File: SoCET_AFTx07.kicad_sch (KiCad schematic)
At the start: 0 parts

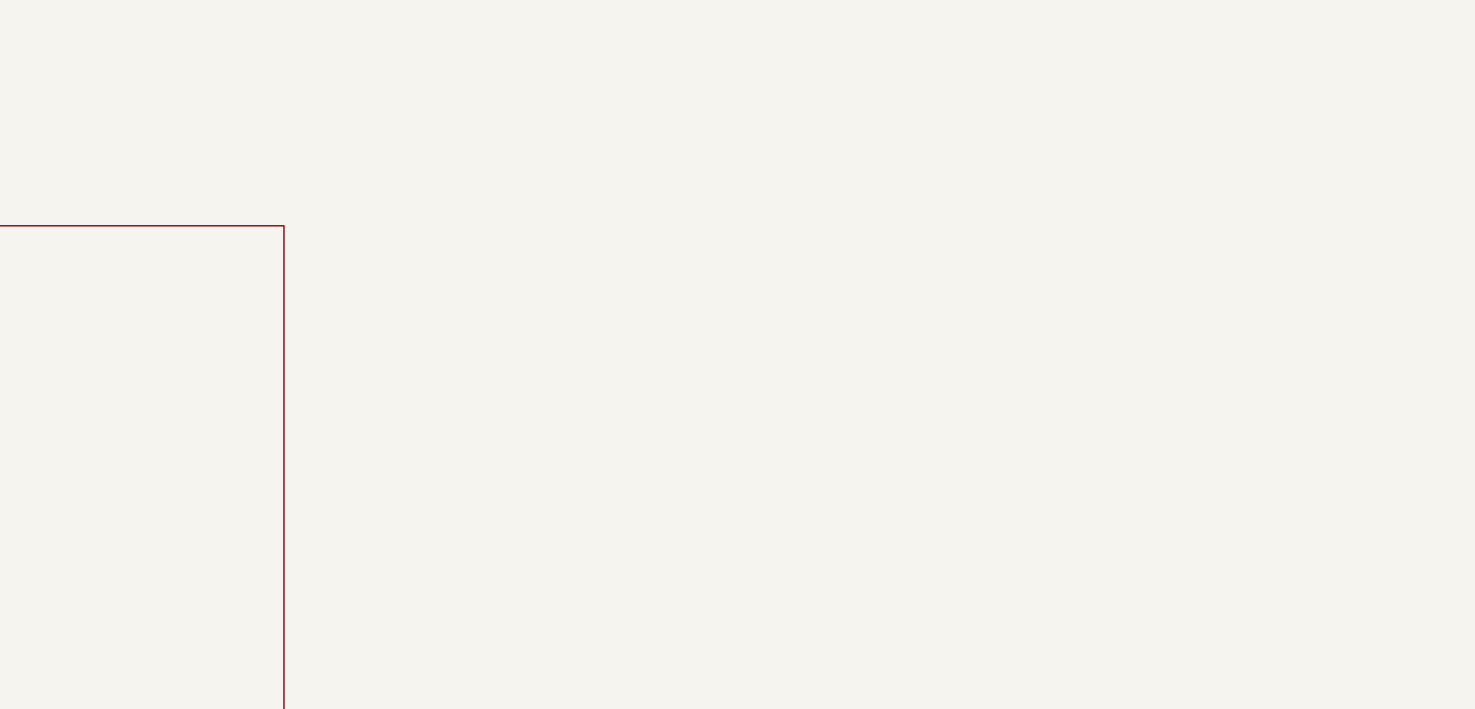
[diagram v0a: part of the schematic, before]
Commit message: Add files via upload
Added sample FMC connector
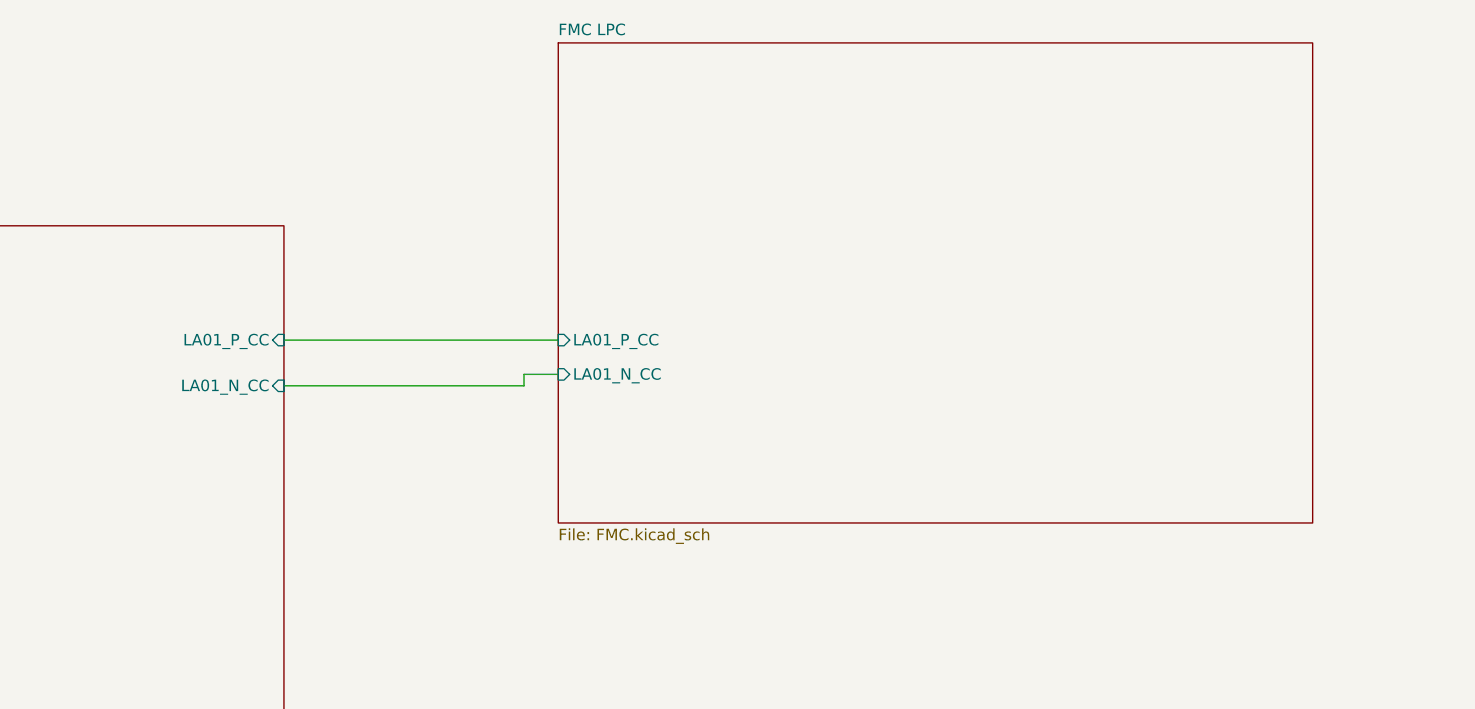
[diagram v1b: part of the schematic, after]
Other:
- added sheet FMC LPC (FMC.kicad_sch)
- sheet AFTx07 ports: added LA01_N_CC, LA01_P_CC; removed none
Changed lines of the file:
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@@
 	(generator_version "8.0")
 	(paper "A4")
+	(wire
+		(pts
+			(xy 171.45 69.85) (xy 175.26 69.85)
+		)
+		(stroke
+			(width 0)
+			(type default)
+		)
+	)
+	(wire
+		(pts
+			(xy 144.78 71.12) (xy 171.45 71.12)
+		)
+		(stroke
+			(width 0)
+			(type default)
+		)
+	)
+	(wire
+		(pts
+			(xy 171.45 71.12) (xy 171.45 69.85)
+		)
+		(stroke
+			(width 0)
+			(type default)
+		)
+	)
+	(wire
+		(pts
+			(xy 144.78 66.04) (xy 175.26 66.04)
+		)
+		(stroke
+			(width 0)
+			(type default)
+		)
+	)
+	(sheet
+		(at 175.26 33.02)
+		(size 83.82 53.34)
+		(fields_autoplaced yes)
+		(stroke
+			(width 0.1524)
+			(type solid)
+		)
+		(fill
+			(color 0 0 0 0.0000)
+		)
+		(property "Sheetname" "FMC LPC"
+			(at 175.26 32.3084 0)
+			(effects
+				(font
+					(size 1.27 1.27)
+				)
+				(justify left bottom)
+			)
+		)
+		(property "Sheetfile" "FMC.kicad_sch"
+			(at 175.26 86.9446 0)
+			(effects
+				(font
+					(size 1.27 1.27)
+				)
+				(justify left top)
+			)
+		)
+		(pin "LA01_P_CC" input
+			(at 175.26 66.04 180)
+			(effects
+				(font
+					(size 1.27 1.27)
+				)
+				(justify left)
+			)
+		)
+		(pin "LA01_N_CC" input
+			(at 175.26 69.85 180)
+			(effects
+				(font
+					(size 1.27 1.27)
+				)
+				(justify left)
+			)
+		)
+		(instances
+			(project "SoCET_AFTx07"
+				(path "/5516d47b-e414-41cc-be39-f34e0b8598e1"
+					(page "4")
+				)
+			)
+		)
+	)
 	(sheet
 		(at 53.34 53.34)
@@
 			)
 		)
+		(pin "LA01_P_CC" input
+			(at 144.78 66.04 0)
+			(effects
+				(font
+					(size 1.27 1.27)
+				)
+				(justify right)
+			)
+		)
+		(pin "LA01_N_CC" input
+			(at 144.78 71.12 0)
+			(effects
+				(font
+					(size 1.27 1.27)
+				)
+				(justify right)
+			)
+		)

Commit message: Add files via upload
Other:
- added sheet Boot (boot.kicad_sch)
- sheet AFTx07 ports: added none; removed LA01_N_CC, LA01_P_CC
- sheet FMC LPC ports: added none; removed LA01_N_CC, LA01_P_CC
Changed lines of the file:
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@@
 	(generator_version "8.0")
 	(paper "A4")
-	(wire
-		(pts
-			(xy 171.45 69.85) (xy 175.26 69.85)
-		)
-		(stroke
-			(width 0)
-			(type default)
-		)
-	)
-	(wire
-		(pts
-			(xy 144.78 71.12) (xy 171.45 71.12)
-		)
-		(stroke
-			(width 0)
-			(type default)
-		)
-	)
-	(wire
-		(pts
-			(xy 171.45 71.12) (xy 171.45 69.85)
-		)
-		(stroke
-			(width 0)
-			(type default)
-		)
-	)
-	(wire
-		(pts
-			(xy 144.78 66.04) (xy 175.26 66.04)
-		)
-		(stroke
-			(width 0)
-			(type default)
-		)
-	)
 	(sheet
 		(at 175.26 33.02)
@@
 			)
 		)
-		(pin "LA01_P_CC" input
-			(at 175.26 66.04 180)
+		(instances
+			(project "SoCET_AFTx07"
+				(path "/5516d47b-e414-41cc-be39-f34e0b8598e1"
+					(page "4")
+				)
+			)
+		)
+	)
+	(sheet
+		(at 44.45 130.81)
+		(size 82.55 45.72)
+		(fields_autoplaced yes)
+		(stroke
+			(width 0.1524)
+			(type solid)
+		)
+		(fill
+			(color 0 0 0 0.0000)
+		)
+		(property "Sheetname" "Boot"
+			(at 44.45 130.0984 0)
 			(effects
 				(font
 					(size 1.27 1.27)
 				)
-				(justify left)
+				(justify left bottom)
 			)
 		)
-		(pin "LA01_N_CC" input
-			(at 175.26 69.85 180)
+		(property "Sheetfile" "boot.kicad_sch"
+			(at 44.45 177.1146 0)
 			(effects
 				(font
 					(size 1.27 1.27)
 				)
-				(justify left)
+				(justify left top)
+			)
+		)
+		(pin "DAT2" input
+			(at 73.66 130.81 90)
+			(effects
+				(font
+					(size 1.27 1.27)
+				)
+				(justify right)
+			)
+		)
+		(pin "DAT3{slash}CD" input
+			(at 78.74 130.81 90)
+			(effects
+				(font
+					(size 1.27 1.27)
+				)
+				(justify right)
+			)
+		)
+		(pin "DAT0" input
+			(at 85.09 130.81 90)
+			(effects
+				(font
+					(size 1.27 1.27)
+				)
+				(justify right)
+			)
+		)
+		(pin "CLK" input
+			(at 91.44 130.81 90)
+			(effects
+				(font
+					(size 1.27 1.27)
+				)
+				(justify right)
+			)
+		)
+		(pin "DAT1" input
+			(at 96.52 130.81 90)
+			(effects
+				(font
+					(size 1.27 1.27)
+				)
+				(justify right)
+			)
+		)
+		(pin "CMD" input
+			(at 101.6 130.81 90)
+			(effects
+				(font
+					(size 1.27 1.27)
+				)
+				(justify right)
 			)
 		)
@@
 			(project "SoCET_AFTx07"
 				(path "/5516d47b-e414-41cc-be39-f34e0b8598e1"
-					(page "4")
+					(page "5")
 				)
 			)
@@
 			)
 		)
-		(pin "LA01_P_CC" input
-			(at 144.78 66.04 0)
-			(effects
-				(font
-					(size 1.27 1.27)
-				)
-				(justify right)
-			)
-		)
-		(pin "LA01_N_CC" input
-			(at 144.78 71.12 0)
-			(effects
-				(font
-					(size 1.27 1.27)
-				)
-				(justify right)
-			)
-		)

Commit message: Add files via upload
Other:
- added sheet power seq (power_seq.kicad_sch)
- sheet AFTx07 ports: added CLK, addr[0..17], data[0..15], gpio[0..31], nCE[0..1], nDB[0..1], nDE[0..1], nLB[0..1], nRST, nWE[0..1], uart.{rx,tx}; removed none
- sheet Boot: file boot.kicad_sch -> Boot.kicad_sch
- sheet FMC LPC ports: added FMC_LA03_N, FMC_LA03_P, FMC_LA05_N, FMC_LA05_P, FMC_LA06_N, FMC_LA06_P, FMC_LA08_N, FMC_LA08_P, FMC_LA09_N, FMC_LA09_P, FMC_LA10_N, FMC_LA10_P, FMC_LA12_N, FMC_LA12_P, FMC_LA13_N, FMC_LA13_P, FMC_LA14_N, FMC_LA14_P, FMC_LA16_N, FMC_LA16_P, FMC_LA18_CC_N, FMC_LA18_CC_P, FMC_LA20_N, FMC_LA20_P, FMC_LA22_N, FMC_LA22_P, FMC_LA23_N, FMC_LA23_P, FMC_LA25_P, FMC_LA27_N, FMC_LA27_P, FMC_LA29_N, FMC_LA29_P, FMC_LA31_N, FMC_LA31_P, FMC_LA33_N, FMC_LA33_P, LA00CCN, LA00CCP, LA01CCN, LA01CCP, LA02N, LA02P, LA04N, LA04P, LA07N, LA07P, LA11N, LA11_P, LA15N, LA15P, LA17CCN, LA17CCP, LA19N, LA19P, LA21N, LA21P, LA24N, LA24P, LA26N, LA26P, LA28N, LA28P, LA30N, LA30P, LA32N, LA32P; removed none
- note added: "addr0"
- note added: "addr1"
- note added: "addr10"
- note added: "addr11"
- note added: "addr12"
- note added: "addr13"
- note added: "addr14"
- note added: "addr15"
- note added: "addr16"
- note added: "addr17"
- note added: "addr2"
- note added: "addr3"
- note added: "addr4"
- note added: "addr5"
- note added: "addr6"
- note added: "addr7"
- note added: "addr8"
- note added: "addr9"

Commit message: Add files via upload
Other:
- removed sheet power seq
- added sheet Power_Sequence (power_seq.kicad_sch)
- sheet AFTx07 ports: added none; removed CLK, addr[0..17], data[0..15], gpio[0..31], nCE[0..1], nDB[0..1], nDE[0..1], nLB[0..1], nRST, nWE[0..1], uart.{rx,tx}
- sheet Boot: file Boot.kicad_sch -> boot.kicad_sch
- sheet FMC LPC ports: added none; removed FMC_LA03_N, FMC_LA03_P, FMC_LA05_N, FMC_LA05_P, FMC_LA06_N, FMC_LA06_P, FMC_LA08_N, FMC_LA08_P, FMC_LA09_N, FMC_LA09_P, FMC_LA10_N, FMC_LA10_P, FMC_LA12_N, FMC_LA12_P, FMC_LA13_N, FMC_LA13_P, FMC_LA14_N, FMC_LA14_P, FMC_LA16_N, FMC_LA16_P, FMC_LA18_CC_N, FMC_LA18_CC_P, FMC_LA20_N, FMC_LA20_P, FMC_LA22_N, FMC_LA22_P, FMC_LA23_N, FMC_LA23_P, FMC_LA25_P, FMC_LA27_N, FMC_LA27_P, FMC_LA29_N, FMC_LA29_P, FMC_LA31_N, FMC_LA31_P, FMC_LA33_N, FMC_LA33_P, LA00CCN, LA00CCP, LA01CCN, LA01CCP, LA02N, LA02P, LA04N, LA04P, LA07N, LA07P, LA11N, LA11_P, LA15N, LA15P, LA17CCN, LA17CCP, LA19N, LA19P, LA21N, LA21P, LA24N, LA24P, LA26N, LA26P, LA28N, LA28P, LA30N, LA30P, LA32N, LA32P
- note removed: "addr0"
- note removed: "addr1"
- note removed: "addr10"
- note removed: "addr11"
- note removed: "addr12"
- note removed: "addr13"
- note removed: "addr14"
- note removed: "addr15"
- note removed: "addr16"
- note removed: "addr17"
- note removed: "addr2"
- note removed: "addr3"
- note removed: "addr4"
- note removed: "addr5"
- note removed: "addr6"
- note removed: "addr7"
- note removed: "addr8"
- note removed: "addr9"
